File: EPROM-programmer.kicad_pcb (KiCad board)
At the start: 4 copper layers, 99.1 x 99.1 mm, 74 parts, among them J1 ZIF-socket, J10 AMP_VPP, J2 ISP, J3 DAC_VCC, J4 DAC_VPP, J5 GND, J6 Barrel_Jack_Switch, J7 ZIF_VCC, J8 AMP_VCC, J9 GND, P1 USB-C, Q1 BC327, Q2 BC327, Q3 BC327, SW1 SW_Push, U1 ATmega1284-P, U2 MCP2221AxP, U3 MCP4812, U4 LM358, U5 ULN2003, U6 LM317_TO-220, U7 LM317_TO-220, Y1 20M

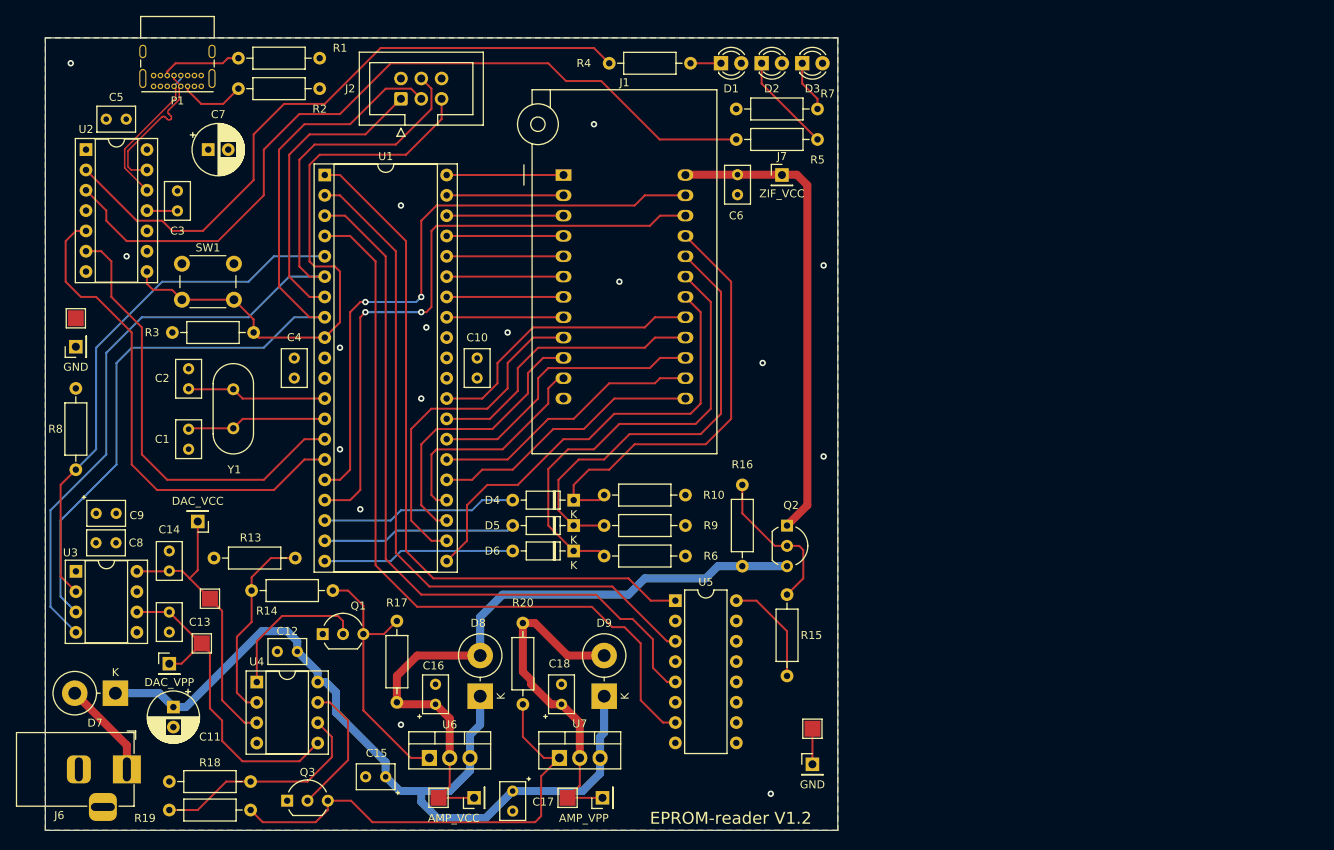
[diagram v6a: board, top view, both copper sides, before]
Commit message: Update schematic with the missing VPP-stuff
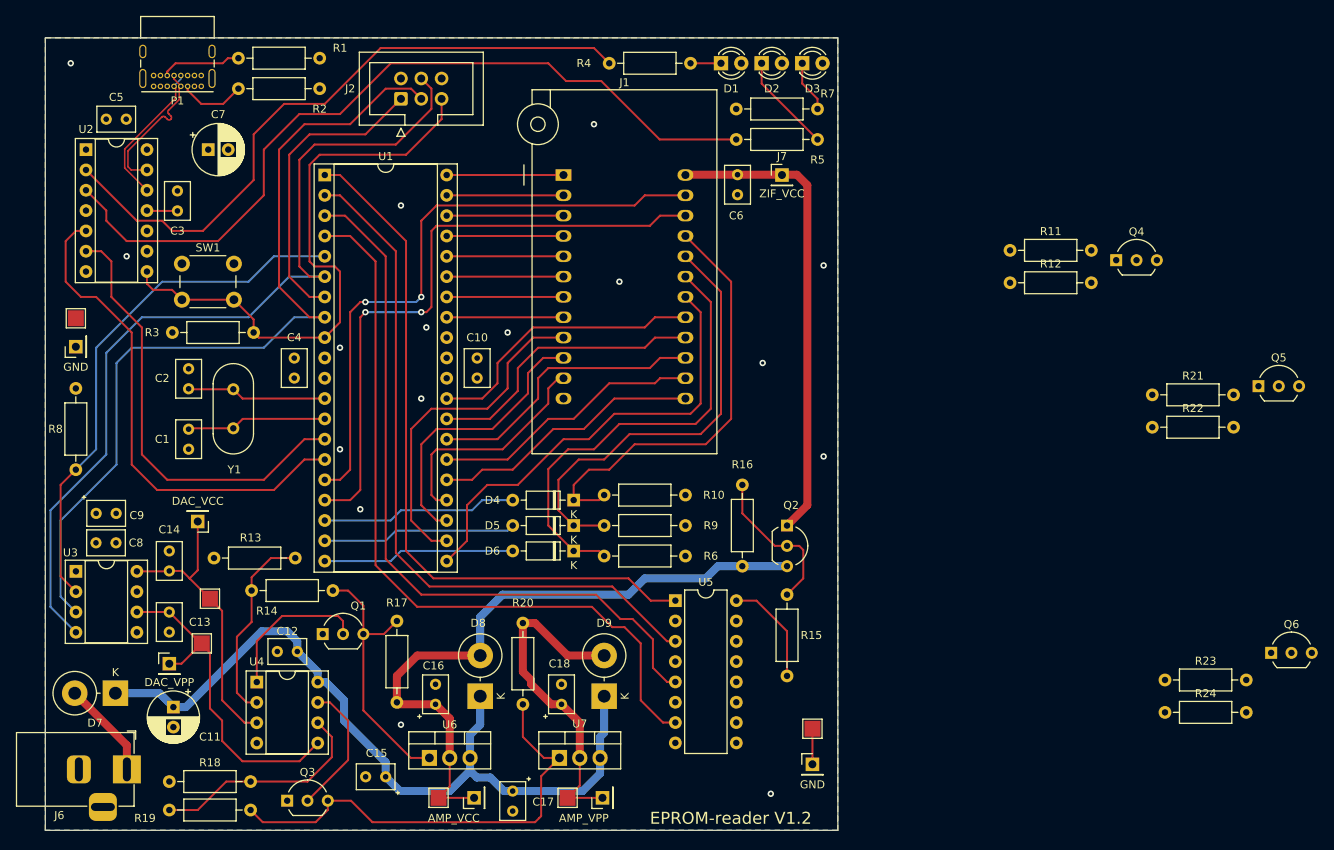
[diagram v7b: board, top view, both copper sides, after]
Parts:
- added Q4: BC327, Package_TO_SOT_THT:TO-92_Inline_Wide, F.Cu at (173.2, 86.2)
- added Q5: BC327, Package_TO_SOT_THT:TO-92_Inline_Wide, F.Cu at (191.0, 102.0)
- added Q6: BC327, Package_TO_SOT_THT:TO-92_Inline_Wide, F.Cu at (192.6, 135.3)
- added R11: 5.1K, Resistor_THT:R_Axial_DIN0207_L6.3mm_D2.5mm_P10.16mm_Horizontal, F.Cu at (160.0, 85.0)
- added R12: 5.1K, Resistor_THT:R_Axial_DIN0207_L6.3mm_D2.5mm_P10.16mm_Horizontal, F.Cu at (160.0, 89.0)
- added R21: 5.1K, Resistor_THT:R_Axial_DIN0207_L6.3mm_D2.5mm_P10.16mm_Horizontal, F.Cu at (177.7, 103.0)
- added R22: 5.1K, Resistor_THT:R_Axial_DIN0207_L6.3mm_D2.5mm_P10.16mm_Horizontal, F.Cu at (177.7, 107.1)
- added R23: 5.1K, Resistor_THT:R_Axial_DIN0207_L6.3mm_D2.5mm_P10.16mm_Horizontal, F.Cu at (179.3, 138.7)
- added R24: 5.1K, Resistor_THT:R_Axial_DIN0207_L6.3mm_D2.5mm_P10.16mm_Horizontal, F.Cu at (179.3, 142.7)
- TP2: value DAC_B_TP -> DAC_VPP_TP
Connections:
- net /ZIF_VPP_P22_EN renamed /ZIF_VPP_P20_EN
- net /ZIF_VPP_P23_EN renamed /ZIF_VPP_P19_EN
- U5 pad 10: unconnected-(U5-O7-Pad10) -> /~{ZIF_VPP_P19_EN}
- U5 pad 12: unconnected-(U5-O5-Pad12) -> /~{ZIF_VPP_P20_EN}
- U5 pad 14: unconnected-(U5-O3-Pad14) -> /~{ZIF_VPP_P21_EN}
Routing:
- net +28V: track 109.5 -> 100.9 mm
